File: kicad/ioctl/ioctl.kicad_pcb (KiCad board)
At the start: 2 copper layers, 37 parts, among them P1 CONN_01X08, P2 CONN_01X08, P3 CONN_01X03, P4 CONN_02X05, P5 CONN_01X08, P6 CONN_02X03, P7 CONN_01X08, U1 74922, U2 74922, U3 CD4021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

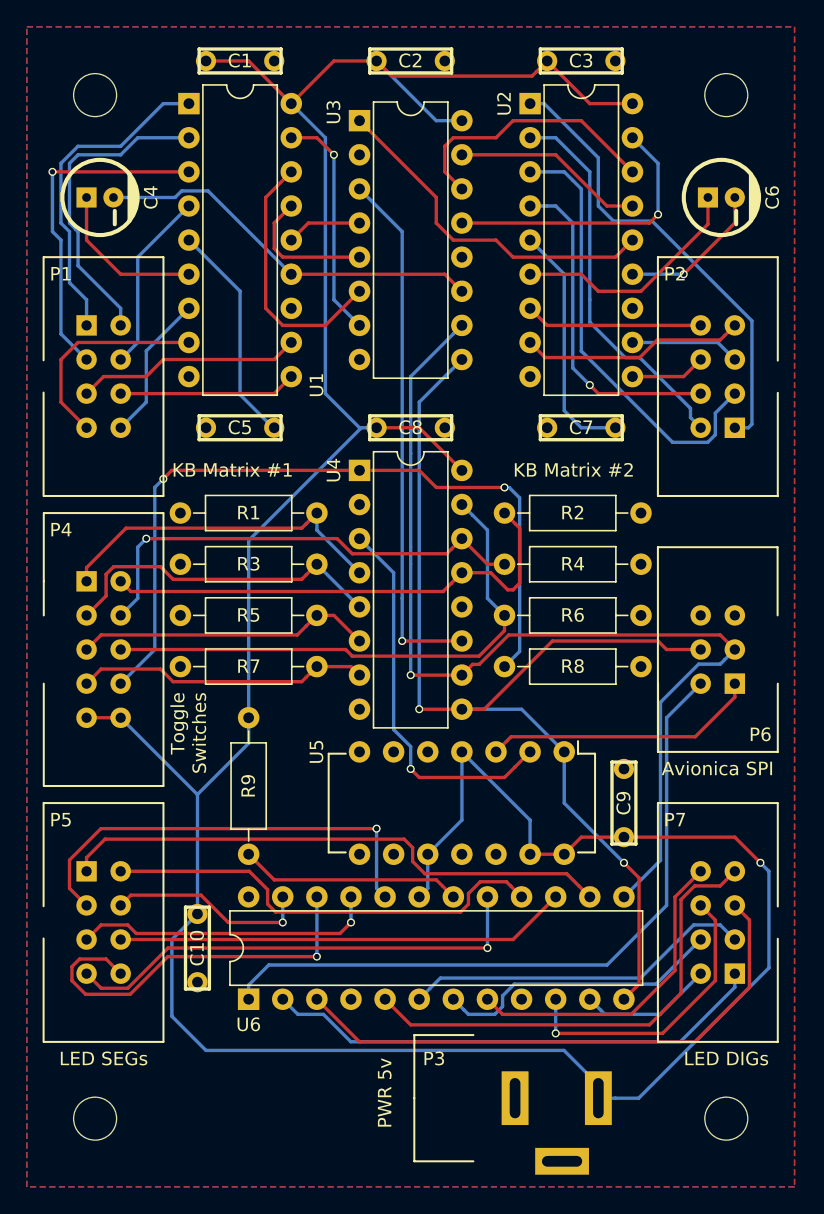
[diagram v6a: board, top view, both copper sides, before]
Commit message: Fix non-DAVed key controllers problem in IO Controller board
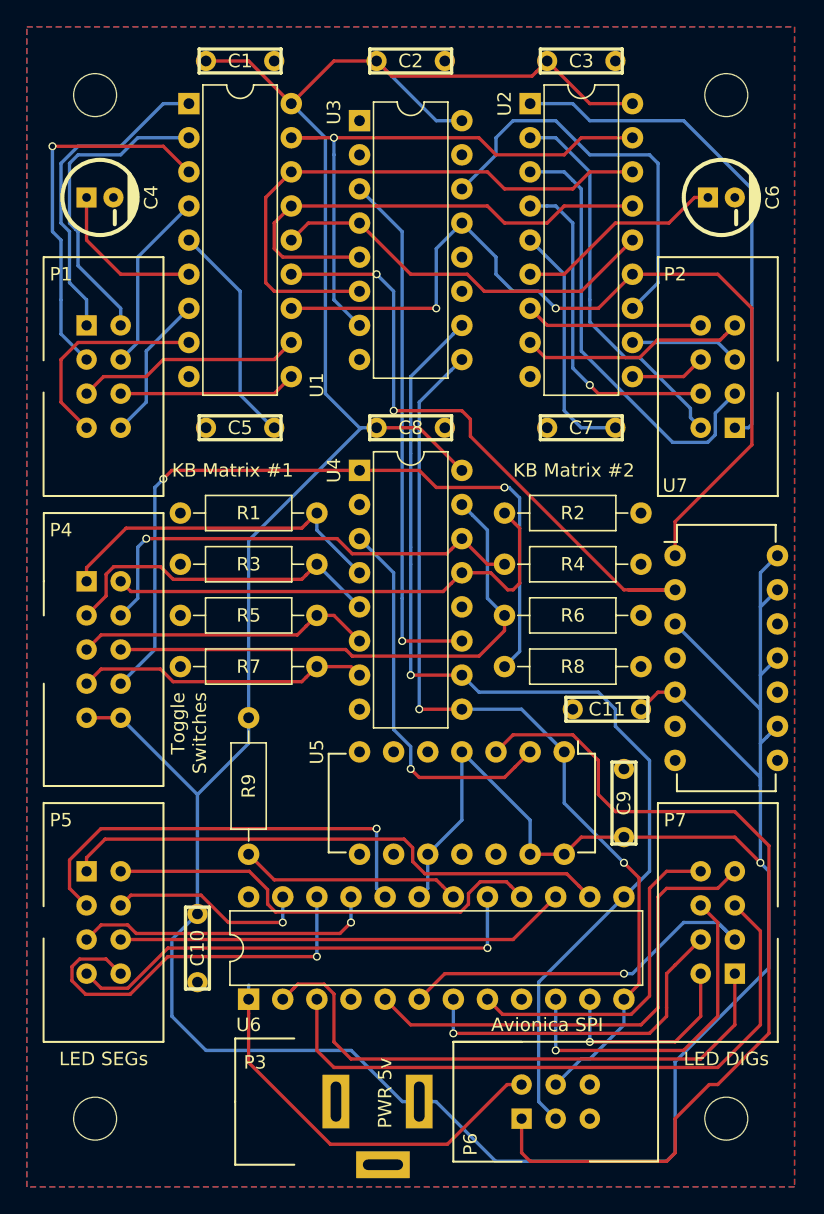
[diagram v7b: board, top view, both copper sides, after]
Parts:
- added C11: 100nF, avionica:Disc_capacitor, F.Cu at (218.4, 81.3)
- added U7: 7404, avionica:DIP-14, F.Cu at (223.5, 69.8)
- moved REF*** 58.9 mm to (188.0, 111.8)
- moved P6 36.1 mm to (212.1, 111.8), turned to 90 degrees
- moved P3 13.3 mm to (201.8, 115.2)
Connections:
- U1 pad 12: (no net) -> Net-(U1-Pad12)
- U1 pad 13: GND -> Net-(U1-Pad13)
- U2 pad 12: (no net) -> Net-(U2-Pad12)
- U2 pad 13: GND -> Net-(U1-Pad12)
- U2 pad 14: Net-(U2-Pad14) -> Net-(U1-Pad14)
- U2 pad 15: Net-(U2-Pad15) -> Net-(U1-Pad15)
- U2 pad 16: Net-(U2-Pad16) -> Net-(U1-Pad16)
- U2 pad 17: Net-(U2-Pad17) -> Net-(U1-Pad17)
- U3 pad 1: Net-(U2-Pad14) -> GND
- U3 pad 13: Net-(U2-Pad17) -> Net-(U1-Pad12)
- U3 pad 14: Net-(U2-Pad16) -> Net-(U2-Pad12)
- U3 pad 15: Net-(U2-Pad15) -> GND
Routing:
- net Net-(U1-Pad12): track 0.00 -> 65.8 mm, vias 0 -> 2
- net VCC: track 240.2 -> 297.9 mm
- net Net-(U1-Pad13): track 0.00 -> 47.7 mm, vias 0 -> 2
- net MISO: track 20.5 -> 66.4 mm
- net GND: track 40.3 -> 0.00 mm, vias 1 -> 0
- net Net-(U2-Pad12): track 0.00 -> 30.4 mm
- net Net-(U1-Pad15): track 10.3 -> 36.8 mm
- net Net-(U2-Pad14): track 26.2 -> 0.00 mm
- net Net-(U1-Pad17): track 17.2 -> 43.1 mm
- net Net-(U1-Pad14): track 5.61 -> 29.6 mm
- net Net-(U1-Pad16): track 19.5 -> 42.7 mm
- net MOSI: track 52.2 -> 30.4 mm
- net Net-(U2-Pad17): track 21.4 -> 0.00 mm, vias 1 -> 0
- net Net-(U2-Pad16): track 20.0 -> 0.00 mm
- net Net-(U2-Pad15): track 14.3 -> 0.00 mm
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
